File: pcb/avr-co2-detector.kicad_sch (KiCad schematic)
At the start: 60 parts, among them J1 USB TYPE-C, J2 LCD0802, J3 AVR-ISP-10, J4 BH1.27-6-2, SW1 "Reset", SW2 "Reset", SW3 "Config", U1 ATtiny2313A-SU, U2 FT232RL, U3 004-0-0053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

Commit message: Added connectors for LCD backlight
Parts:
- added J2, J3: Backlight, Connector_PinHeader_2.54mm:PinHeader_1x01_P2.54mm_Vertical, symbol Connector_Generic:Conn_01x01
- renumbered J2 to J4, J3 to J5, J4 to J6
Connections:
- net GND: now also J3.1 (Pin_1)
- net LED+: now also J2.1 (Pin_1)
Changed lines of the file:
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@@
   (junction (at 293.37 144.78) (diameter 0) (color 0 0 0 0)
   )
+  (junction (at 114.3 182.88) (diameter 0) (color 0 0 0 0)
+  )
   (junction (at 266.7 101.6) (diameter 0) (color 0 0 0 0)
   )
@@
   (junction (at 85.09 95.25) (diameter 0) (color 0 0 0 0)
   )
+  (junction (at 127 182.88) (diameter 0) (color 0 0 0 0)
+  )
   (wire (pts (xy 237.49 165.1) (xy 237.49 166.37))
     (stroke (width 0) (type default) (color 0 0 0 0))
@@
     (stroke (width 0) (type default) (color 0 0 0 0))
   )
+  (wire (pts (xy 113.03 182.88) (xy 113.03 189.23))
+    (stroke (width 0) (type default) (color 0 0 0 0))
+  )
   (wire (pts (xy 255.27 88.9) (xy 256.54 88.9))
     (stroke (width 0) (type default) (color 0 0 0 0))
@@
     (stroke (width 0) (type default) (color 0 0 0 0))
   )
+  (wire (pts (xy 119.38 185.42) (xy 127 185.42))
+    (stroke (width 0) (type default) (color 0 0 0 0))
+  )
   (wire (pts (xy 100.33 158.75) (xy 102.87 158.75))
     (stroke (width 0) (type default) (color 0 0 0 0))
@@
     (stroke (width 0) (type default) (color 0 0 0 0))
   )
+  (wire (pts (xy 127 182.88) (xy 127 185.42))
+    (stroke (width 0) (type default) (color 0 0 0 0))
+  )
   (wire (pts (xy 43.18 125.73) (xy 43.18 135.89))
     (stroke (width 0) (type default) (color 0 0 0 0))
@@
     (stroke (width 0) (type default) (color 0 0 0 0))
   )
+  (wire (pts (xy 113.03 189.23) (xy 110.49 189.23))
+    (stroke (width 0) (type default) (color 0 0 0 0))
+  )
   (wire (pts (xy 102.87 100.33) (xy 102.87 125.73))
     (stroke (width 0) (type default) (color 0 0 0 0))
@@
     (stroke (width 0) (type default) (color 0 0 0 0))
   )
+  (wire (pts (xy 119.38 194.31) (xy 119.38 185.42))
+    (stroke (width 0) (type default) (color 0 0 0 0))
+  )
   (wire (pts (xy 201.93 43.18) (xy 189.23 43.18))
     (stroke (width 0) (type default) (color 0 0 0 0))
@@
     (stroke (width 0) (type default) (color 0 0 0 0))
   )
+  (wire (pts (xy 101.6 194.31) (xy 119.38 194.31))
+    (stroke (width 0) (type default) (color 0 0 0 0))
+  )
   (wire (pts (xy 104.14 101.6) (xy 104.14 128.27))
     (stroke (width 0) (type default) (color 0 0 0 0))
@@
     (stroke (width 0) (type default) (color 0 0 0 0))
   )
+  (wire (pts (xy 113.03 182.88) (xy 114.3 182.88))
+    (stroke (width 0) (type default) (color 0 0 0 0))
+  )
   (wire (pts (xy 43.18 125.73) (xy 45.72 125.73))
     (stroke (width 0) (type default) (color 0 0 0 0))
@@
     (pin "1")
   )
+  (symbol (lib_id "Connector_Generic:Conn_01x01") (at 96.52 194.31 180) (unit 1)
+    (in_bom yes) (on_board yes) (fields_autoplaced)
+    (property "Reference" "J2" (id 0) (at 96.52 187.96 0))
+    (property "Value" "Backlight" (id 1) (at 96.52 190.5 0))
+    (property "Footprint" "Connector_PinHeader_2.54mm:PinHeader_1x01_P2.54mm_Vertical" (id 2) (at 96.52 194.31 0)
+      (effects (font (size 1.27 1.27)) hide)
+    )
+    (property "Datasheet" "~" (id 3) (at 96.52 194.31 0)
+      (effects (font (size 1.27 1.27)) hide)
+    )
+    (pin "1")
+  )
   (symbol (lib_id "Device:C_Small") (at 110.49 44.45 90) (unit 1)
     (in_bom yes) (on_board yes) (fields_autoplaced)
@@
     (pin "2")
   )
+  (symbol (lib_id "Connector_Generic:Conn_01x01") (at 105.41 189.23 180) (unit 1)
+    (in_bom yes) (on_board yes) (fields_autoplaced)
+    (property "Reference" "J3" (id 0) (at 105.41 182.88 0))
+    (property "Value" "Backlight" (id 1) (at 105.41 185.42 0))
+    (property "Footprint" "Connector_PinHeader_2.54mm:PinHeader_1x01_P2.54mm_Vertical" (id 2) (at 105.41 189.23 0)
+      (effects (font (size 1.27 1.27)) hide)
+    )
+    (property "Datasheet" "~" (id 3) (at 105.41 189.23 0)
+      (effects (font (size 1.27 1.27)) hide)
+    )
+    (pin "1")
+  )
   (symbol (lib_id "Connector_Generic:Conn_02x08_Odd_Even") (at 119.38 172.72 0) (unit 1)
     (in_bom yes) (on_board yes)
-    (property "Reference" "J2" (id 0) (at 120.65 160.02 0))
+    (property "Reference" "J4" (id 0) (at 120.65 160.02 0))
     (property "Value" "LCD0802" (id 1) (at 120.65 162.56 0))
     (property "Footprint" "Connector_IDC:IDC-Header_2x08_P2.54mm_Vertical" (id 2) (at 119.38 172.72 0)
@@
   (symbol (lib_id "Connector_Generic:Conn_02x03_Odd_Even") (at 289.56 96.52 0) (unit 1)
     (in_bom yes) (on_board yes) (fields_autoplaced)
-    (property "Reference" "J4" (id 0) (at 290.83 87.63 0))
+    (property "Reference" "J6" (id 0) (at 290.83 87.63 0))
     (property "Value" "BH1.27-6-2" (id 1) (at 290.83 90.17 0))
     (property "Footprint" "Connector:Tag-Connect_TC2030-IDC-NL_2x03_P1.27mm_Vertical" (id 2) (at 289.56 96.52 0)
@@
   (symbol (lib_id "Connector:AVR-ISP-10") (at 124.46 123.19 180) (unit 1)
     (in_bom yes) (on_board yes) (fields_autoplaced)
-    (property "Reference" "J3" (id 0) (at 133.35 123.1899 0)
+    (property "Reference" "J5" (id 0) (at 133.35 123.1899 0)
       (effects (font (size 1.27 1.27)) (justify right))
     )
@@
       (reference "J1") (unit 1) (value "USB TYPE-C") (footprint "Connector_USB:USB_C_Receptacle_HRO_TYPE-C-31-M-12")
     )
+    (path "/0836868e-c0ed-46e2-92bc-ac2d5070939f"
+      (reference "J2") (unit 1) (value "Backlight") (footprint "Connector_PinHeader_2.54mm:PinHeader_1x01_P2.54mm_Vertical")
+    )
+    (path "/0a298738-f98c-47b2-b5f4-68911fe601cc"
+      (reference "J3") (unit 1) (value "Backlight") (footprint "Connector_PinHeader_2.54mm:PinHeader_1x01_P2.54mm_Vertical")
+    )
     (path "/0b11e975-2d63-469f-9490-cfb160f62e89"
-      (reference "J2") (unit 1) (value "LCD0802") (footprint "Connector_IDC:IDC-Header_2x08_P2.54mm_Vertical")
+      (reference "J4") (unit 1) (value "LCD0802") (footprint "Connector_IDC:IDC-Header_2x08_P2.54mm_Vertical")
     )
     (path "/e2b21b53-c0d7-4243-8edc-aa486abb73ae"
-      (reference "J3") (unit 1) (value "AVR-ISP-10") (footprint "Connector_IDC:IDC-Header_2x05_P2.54mm_Vertical")
+      (reference "J5") (unit 1) (value "AVR-ISP-10") (footprint "Connector_IDC:IDC-Header_2x05_P2.54mm_Vertical")
     )
     (path "/7331dd53-b74c-407d-99f2-d04a0d92ca38"
-      (reference "J4") (unit 1) (value "BH1.27-6-2") (footprint "Connector:Tag-Connect_TC2030-IDC-NL_2x03_P1.27mm_Vertical")
+      (reference "J6") (unit 1) (value "BH1.27-6-2") (footprint "Connector:Tag-Connect_TC2030-IDC-NL_2x03_P1.27mm_Vertical")
     )
     (path "/bade648f-7468-4843-9b05-5a4d92a200c5"

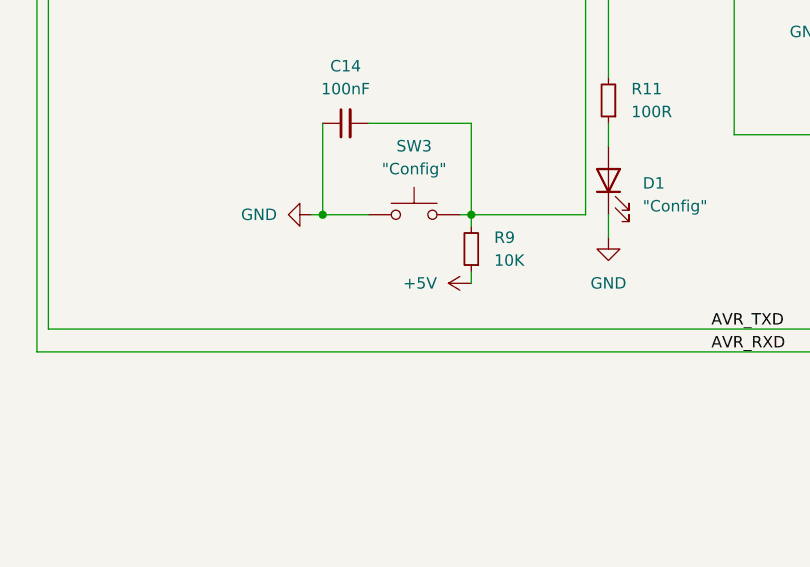
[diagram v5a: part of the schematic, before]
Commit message: Corrected pull-up voltage on resistor R9, corrected footprint for connector J6
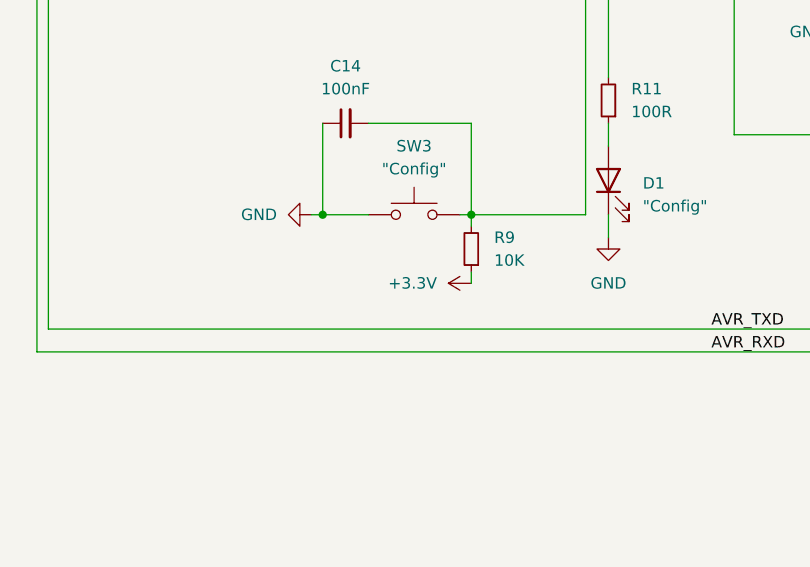
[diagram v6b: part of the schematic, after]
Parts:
- J6: footprint Connector:Tag-Connect_TC2030-IDC-NL_2x03_P1.27mm_Vertical -> Connector_PinHeader_1.27mm:PinHeader_2x03_P1.27mm_Vertical
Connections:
- net +3.3V: now also R9.1
- net +5V: no longer R9.1
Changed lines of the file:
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@@
     (pin "2")
+  )
+  (symbol (lib_id "power:+3.3V") (at 237.49 172.72 90) (unit 1)
+    (in_bom yes) (on_board yes) (fields_autoplaced)
+    (property "Reference" "#PWR?" (id 0) (at 241.3 172.72 0)
+      (effects (font (size 1.27 1.27)) hide)
+    )
+    (property "Value" "+3.3V" (id 1) (at 233.68 172.7199 90)
+      (effects (font (size 1.27 1.27)) (justify left))
+    )
+    (property "Footprint" "" (id 2) (at 237.49 172.72 0)
+      (effects (font (size 1.27 1.27)) hide)
+    )
+    (property "Datasheet" "" (id 3) (at 237.49 172.72 0)
+      (effects (font (size 1.27 1.27)) hide)
+    )
+    (pin "1")
   )
   (symbol (lib_id "Logic_LevelTranslator:SN74LVC1T45DBV") (at 341.63 58.42 0) (unit 1)
@@
     (pin "2")
   )
-  (symbol (lib_id "power:+5V") (at 237.49 172.72 90) (unit 1)
-    (in_bom yes) (on_board yes) (fields_autoplaced)
-    (property "Reference" "#PWR030" (id 0) (at 241.3 172.72 0)
-      (effects (font (size 1.27 1.27)) hide)
-    )
-    (property "Value" "+5V" (id 1) (at 233.68 172.7199 90)
-      (effects (font (size 1.27 1.27)) (justify left))
-    )
-    (property "Footprint" "" (id 2) (at 237.49 172.72 0)
-      (effects (font (size 1.27 1.27)) hide)
-    )
-    (property "Datasheet" "" (id 3) (at 237.49 172.72 0)
-      (effects (font (size 1.27 1.27)) hide)
-    )
-    (pin "1")
-  )
   (symbol (lib_id "Device:R_Small") (at 252.73 152.4 180) (unit 1)
     (in_bom yes) (on_board yes) (fields_autoplaced)
@@
     (property "Reference" "J6" (id 0) (at 290.83 87.63 0))
     (property "Value" "BH1.27-6-2" (id 1) (at 290.83 90.17 0))
-    (property "Footprint" "Connector:Tag-Connect_TC2030-IDC-NL_2x03_P1.27mm_Vertical" (id 2) (at 289.56 96.52 0)
+    (property "Footprint" "Connector_PinHeader_1.27mm:PinHeader_2x03_P1.27mm_Vertical" (id 2) (at 289.56 96.52 0)
       (effects (font (size 1.27 1.27)) hide)
     )
@@
       (reference "#PWR029") (unit 1) (value "GND") (footprint "")
     )
-    (path "/605fbb56-8da3-4aef-9b1f-2e590b9cdadb"
-      (reference "#PWR030") (unit 1) (value "+5V") (footprint "")
-    )
     (path "/29ada418-1fd3-4155-a2b6-64a1493d8106"
       (reference "#PWR031") (unit 1) (value "GND") (footprint "")
@@
       (reference "#PWR054") (unit 1) (value "GND") (footprint "")
     )
+    (path "/3ce18ad5-c25f-473d-96d7-76d865186ed1"
+      (reference "#PWR?") (unit 1) (value "+3.3V") (footprint "")
+    )
     (path "/9027a3cb-d61e-47fa-a79d-fba2d8e0022e"
       (reference "C1") (unit 1) (value "100nF") (footprint "Capacitor_SMD:C_0805_2012Metric_Pad1.18x1.45mm_HandSolder")
@@
     )
     (path "/7331dd53-b74c-407d-99f2-d04a0d92ca38"
-      (reference "J6") (unit 1) (value "BH1.27-6-2") (footprint "Connector:Tag-Connect_TC2030-IDC-NL_2x03_P1.27mm_Vertical")
+      (reference "J6") (unit 1) (value "BH1.27-6-2") (footprint "Connector_PinHeader_1.27mm:PinHeader_2x03_P1.27mm_Vertical")
     )
     (path "/bade648f-7468-4843-9b05-5a4d92a200c5"
